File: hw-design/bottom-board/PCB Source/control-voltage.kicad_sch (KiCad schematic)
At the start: 52 parts, among them J16 NYS215, J17 NYS215, U10 LM358, U13 DG9426E, U20 ADC122S021, U21 MIC2076A, U24 MCP4922-EP, U3 74LVC3G17, U4 LD1117S50TR, U9 DG9426E

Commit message: change U21 (EXP supply) MPN, due to unavailabilaty again
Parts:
- U21: MPN2 (none) -> SP2526A-1EN-L/TR
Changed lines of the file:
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@@
+      (effects (font (size 1.524 1.524)) hide)
+    )
+    (property "MPN2" "SP2526A-1EN-L/TR" (id 5) (at 103.759 129.8194 0)
       (effects (font (size 1.524 1.524)) hide)
     )

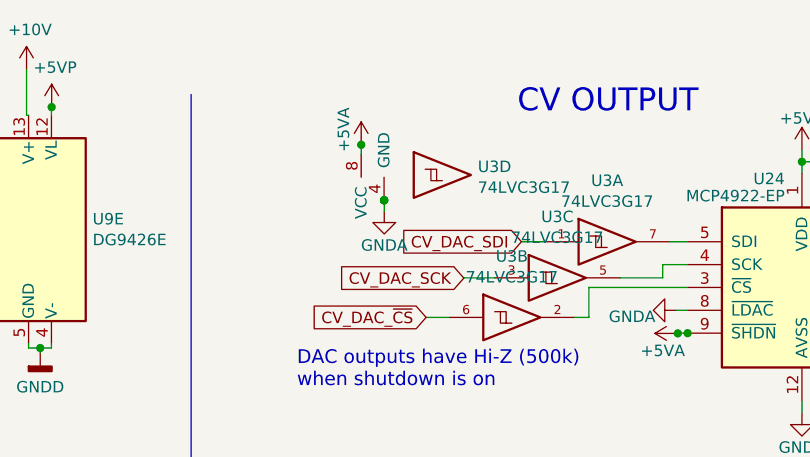
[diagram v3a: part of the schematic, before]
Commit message: fix issues reported by Kicad 6 RDC
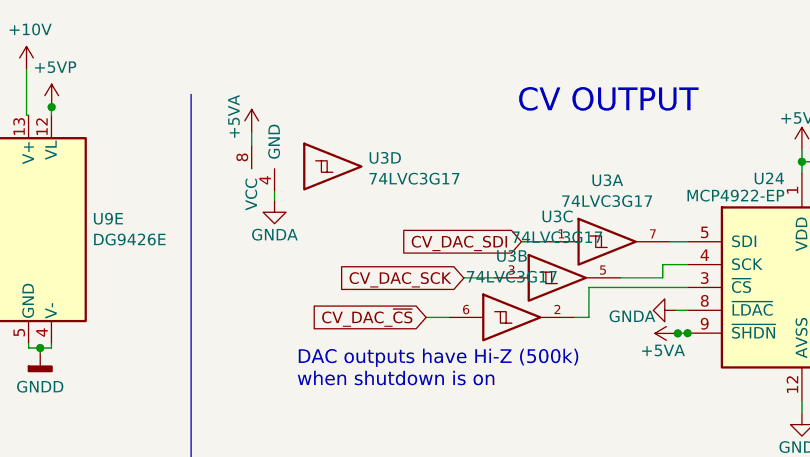
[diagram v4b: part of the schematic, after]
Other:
- moved on the sheet: U3D
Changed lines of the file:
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@@
   (junction (at 244.3988 37.3126) (diameter 0) (color 0 0 0 0)
   )
-  (junction (at 176.3776 32.7152) (diameter 0) (color 0 0 0 0)
-  )
   (junction (at 100.711 171.069) (diameter 0) (color 0 0 0 0)
   )
@@
   (junction (at 196.3674 77.9018) (diameter 0) (color 0 0 0 0)
   )
-  (junction (at 176.3776 32.6898) (diameter 0) (color 0 0 0 0)
-  )
   (junction (at 103.759 143.764) (diameter 0) (color 0 0 0 0)
   )
@@
   (junction (at 244.3988 25.8826) (diameter 0) (color 0 0 0 0)
   )
-  (junction (at 176.403 32.7152) (diameter 0) (color 0 0 0 0)
-  )
   (junction (at 248.793 64.7954) (diameter 0) (color 0 0 0 0)
   )
@@
   )
   (junction (at 101.219 188.468) (diameter 0) (color 0 0 0 0)
-  )
-  (junction (at 173.8376 26.543) (diameter 0) (color 0 0 0 0)
   )
   (no_connect (at 271.272 163.322))
@@
     (stroke (width 0) (type default) (color 0 0 0 0))
   )
-  (wire (pts (xy 173.8376 26.4668) (xy 173.8376 26.543))
-    (stroke (width 0) (type default) (color 0 0 0 0))
-  )
   (wire (pts (xy 67.31 93.98) (xy 67.31 95.25))
     (stroke (width 0) (type default) (color 0 0 0 0))
@@
     (stroke (width 0) (type default) (color 0 0 0 0))
   )
-  (wire (pts (xy 176.3776 32.7152) (xy 176.3776 32.6898))
-    (stroke (width 0) (type default) (color 0 0 0 0))
-  )
   (wire (pts (xy 113.919 126.0094) (xy 125.984 126.0094))
     (stroke (width 0) (type default) (color 0 0 0 0))
@@
     (stroke (width 0) (type default) (color 0 0 0 0))
   )
-  (wire (pts (xy 176.403 33.909) (xy 176.403 32.7152))
-    (stroke (width 0) (type default) (color 0 0 0 0))
-  )
   (wire (pts (xy 92.329 122.1994) (xy 93.599 122.1994))
     (stroke (width 0) (type default) (color 0 0 0 0))
@@
     (stroke (width 0) (type default) (color 0 0 0 0))
   )
+  (wire (pts (xy 164.211 31.75) (xy 164.211 32.766))
+    (stroke (width 0) (type default) (color 0 0 0 0))
+  )
   (wire (pts (xy 209.0166 47.4726) (xy 209.0166 47.498))
     (stroke (width 0) (type default) (color 0 0 0 0))
@@
     (stroke (width 0) (type default) (color 0 0 0 0))
   )
-  (wire (pts (xy 173.8376 26.543) (xy 173.8376 27.6098))
-    (stroke (width 0) (type default) (color 0 0 0 0))
-  )
   (wire (pts (xy 84.8106 126.7206) (xy 84.8106 129.8194))
     (stroke (width 0) (type default) (color 0 0 0 0))
@@
     (stroke (width 0) (type default) (color 0 0 0 0))
   )
+  (wire (pts (xy 161.671 25.146) (xy 161.671 26.67))
+    (stroke (width 0) (type default) (color 0 0 0 0))
+  )
   (wire (pts (xy 39.243 98.9076) (xy 37.338 98.9076))
     (stroke (width 0) (type default) (color 0 0 0 0))
@@
   )
   (wire (pts (xy 101.219 188.468) (xy 99.187 188.468))
-    (stroke (width 0) (type default) (color 0 0 0 0))
-  )
-  (wire (pts (xy 176.403 32.7152) (xy 176.3776 32.7152))
     (stroke (width 0) (type default) (color 0 0 0 0))
   )
@@
     (pin "5")
   )
-  (symbol (lib_id "74xGxx_local:74LVC3G17") (at 183.4896 29.8958 0) (unit 4)
-    (in_bom yes) (on_board yes)
-    (property "Reference" "U3" (id 0) (at 186.7916 28.9814 0)
-      (effects (font (size 1.27 1.27)) (justify left))
-    )
-    (property "Value" "74LVC3G17" (id 1) (at 186.7916 31.2928 0)
-      (effects (font (size 1.27 1.27)) (justify left))
-    )
-    (property "Footprint" "Package_SO:VSSOP-8_2.3x2mm_P0.5mm" (id 2) (at 183.4896 29.8958 0)
-      (effects (font (size 1.27 1.27)) hide)
-    )
-    (property "Datasheet" "" (id 3) (at 183.4896 29.8958 0)
-      (effects (font (size 1.27 1.27)) hide)
-    )
-    (property "MPN" "SN74LVC3G17DCUR" (id 4) (at 183.4896 29.8958 0)
+  (symbol (lib_id "74xGxx_local:74LVC3G17") (at 171.323 28.956 0) (unit 4)
+    (in_bom yes) (on_board yes)
+    (property "Reference" "U3" (id 0) (at 174.625 28.0416 0)
+      (effects (font (size 1.27 1.27)) (justify left))
+    )
+    (property "Value" "74LVC3G17" (id 1) (at 174.625 30.353 0)
+      (effects (font (size 1.27 1.27)) (justify left))
+    )
+    (property "Footprint" "Package_SO:VSSOP-8_2.3x2mm_P0.5mm" (id 2) (at 171.323 28.956 0)
+      (effects (font (size 1.27 1.27)) hide)
+    )
+    (property "Datasheet" "" (id 3) (at 171.323 28.956 0)
+      (effects (font (size 1.27 1.27)) hide)
+    )
+    (property "MPN" "SN74LVC3G17DCUR" (id 4) (at 171.323 28.956 0)
       (effects (font (size 1.27 1.27)) hide)
     )
@@
     (pin "8")
   )
-  (symbol (lib_id "bottom-board-rescue:+5VA-power") (at 173.8376 26.543 0) (mirror y) (unit 1)
-    (in_bom yes) (on_board yes)
-    (property "Reference" "#PWR0305" (id 0) (at 173.8376 30.353 0)
-      (effects (font (size 1.27 1.27)) hide)
-    )
-    (property "Value" "+5VA" (id 1) (at 171.9072 24.8666 90))
-    (property "Footprint" "" (id 2) (at 173.8376 26.543 0)
-      (effects (font (size 1.524 1.524)))
-    )
-    (property "Datasheet" "" (id 3) (at 173.8376 26.543 0)
-      (effects (font (size 1.524 1.524)))
-    )
-    (pin "1")
-  )
-  (symbol (lib_id "bottom-board-rescue:GNDA-power") (at 176.403 33.909 0) (unit 1)
-    (in_bom yes) (on_board yes)
-    (property "Reference" "#PWR0310" (id 0) (at 176.403 40.259 0)
-      (effects (font (size 1.27 1.27)) hide)
-    )
-    (property "Value" "GNDA" (id 1) (at 176.403 37.719 0))
-    (property "Footprint" "" (id 2) (at 176.403 33.909 0)
-      (effects (font (size 1.524 1.524)))
-    )
-    (property "Datasheet" "" (id 3) (at 176.403 33.909 0)
-      (effects (font (size 1.524 1.524)))
-    )
+  (symbol (lib_id "bottom-board-rescue:+5VA-power") (at 161.671 25.146 0) (mirror y) (unit 1)
+    (in_bom yes) (on_board yes)
+    (property "Reference" "#PWR0305" (id 0) (at 161.671 28.956 0)
+      (effects (font (size 1.27 1.27)) hide)
+    )
+    (property "Value" "+5VA" (id 1) (at 159.7406 23.4696 90))
+    (property "Footprint" "" (id 2) (at 161.671 25.146 0)
+      (effects (font (size 1.524 1.524)))
+    )
+    (property "Datasheet" "" (id 3) (at 161.671 25.146 0)
+      (effects (font (size 1.524 1.524)))
+    )
+    (pin "1")
+  )
+  (symbol (lib_id "bottom-board-rescue:GNDA-power") (at 164.211 32.766 0) (unit 1)
+    (in_bom yes) (on_board yes)
+    (property "Reference" "#PWR0310" (id 0) (at 164.211 39.116 0)
+      (effects (font (size 1.27 1.27)) hide)
+    )
+    (property "Value" "GNDA" (id 1) (at 164.211 36.576 0))
+    (property "Footprint" "" (id 2) (at 164.211 32.766 0)
+      (effects (font (size 1.524 1.524)))
+    )
+    (property "Datasheet" "" (id 3) (at 164.211 32.766 0)
+      (effects (font (size 1.524 1.524)))
+    )

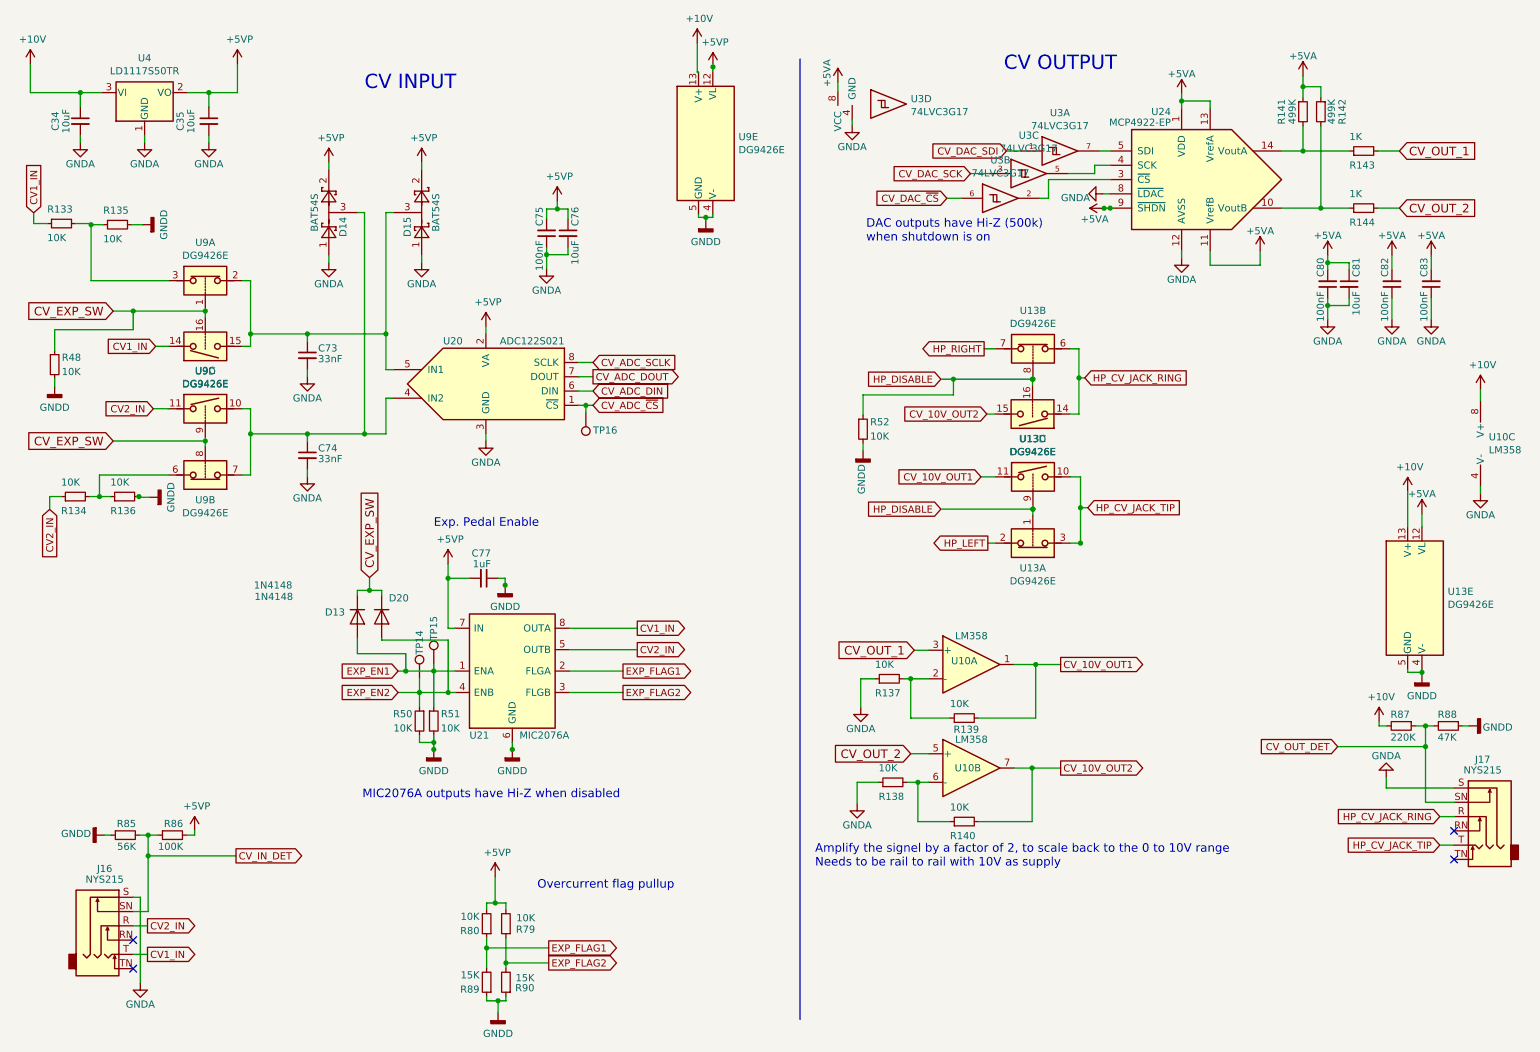
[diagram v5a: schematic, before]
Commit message: mainboard: correct CC TX pin + update fabrication files
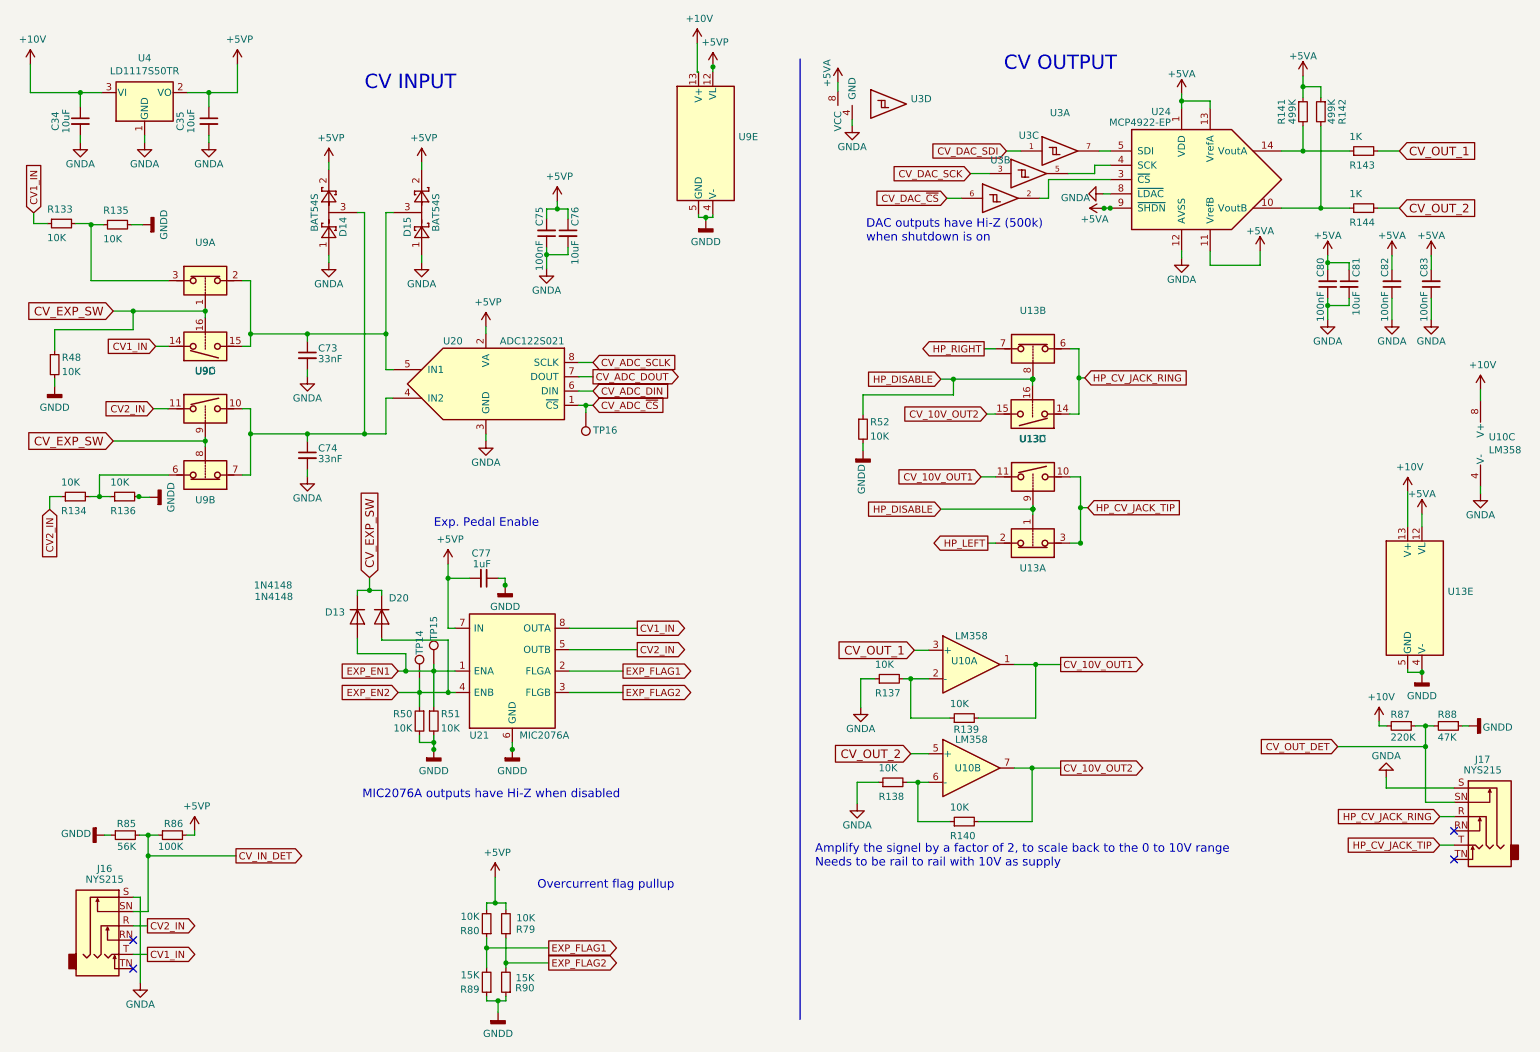
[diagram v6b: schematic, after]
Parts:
- U13, U9: value DG9426E -> (none); footprint Package_SO:TSSOP-16_4.4x5mm_P0.65mm -> (none)
- U13, U9: value DG9426E -> (none); footprint Package_SO:TSSOP-16_4.4x5mm_P0.65mm -> (none); MPN (none) -> DG9426EDQ-T1-GE3
- U13: value DG9426E -> (none); footprint Package_SO:TSSOP-16_4.4x5mm_P0.65mm -> (none); MPN LM358DGKR -> DG9426EDQ-T1-GE3
- U3: value 74LVC3G17 -> (none); footprint Package_SO:VSSOP-8_2.3x2mm_P0.5mm -> (none); MPN2 (none) -> 74LVC3G17
